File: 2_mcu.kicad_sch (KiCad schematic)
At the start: 33 parts, among them J201 Conn_01x05_Pin, J202 SWD TagConnect, SW201 PTS810 SJK, U201 STM32F446RETx, Y201 16MHz

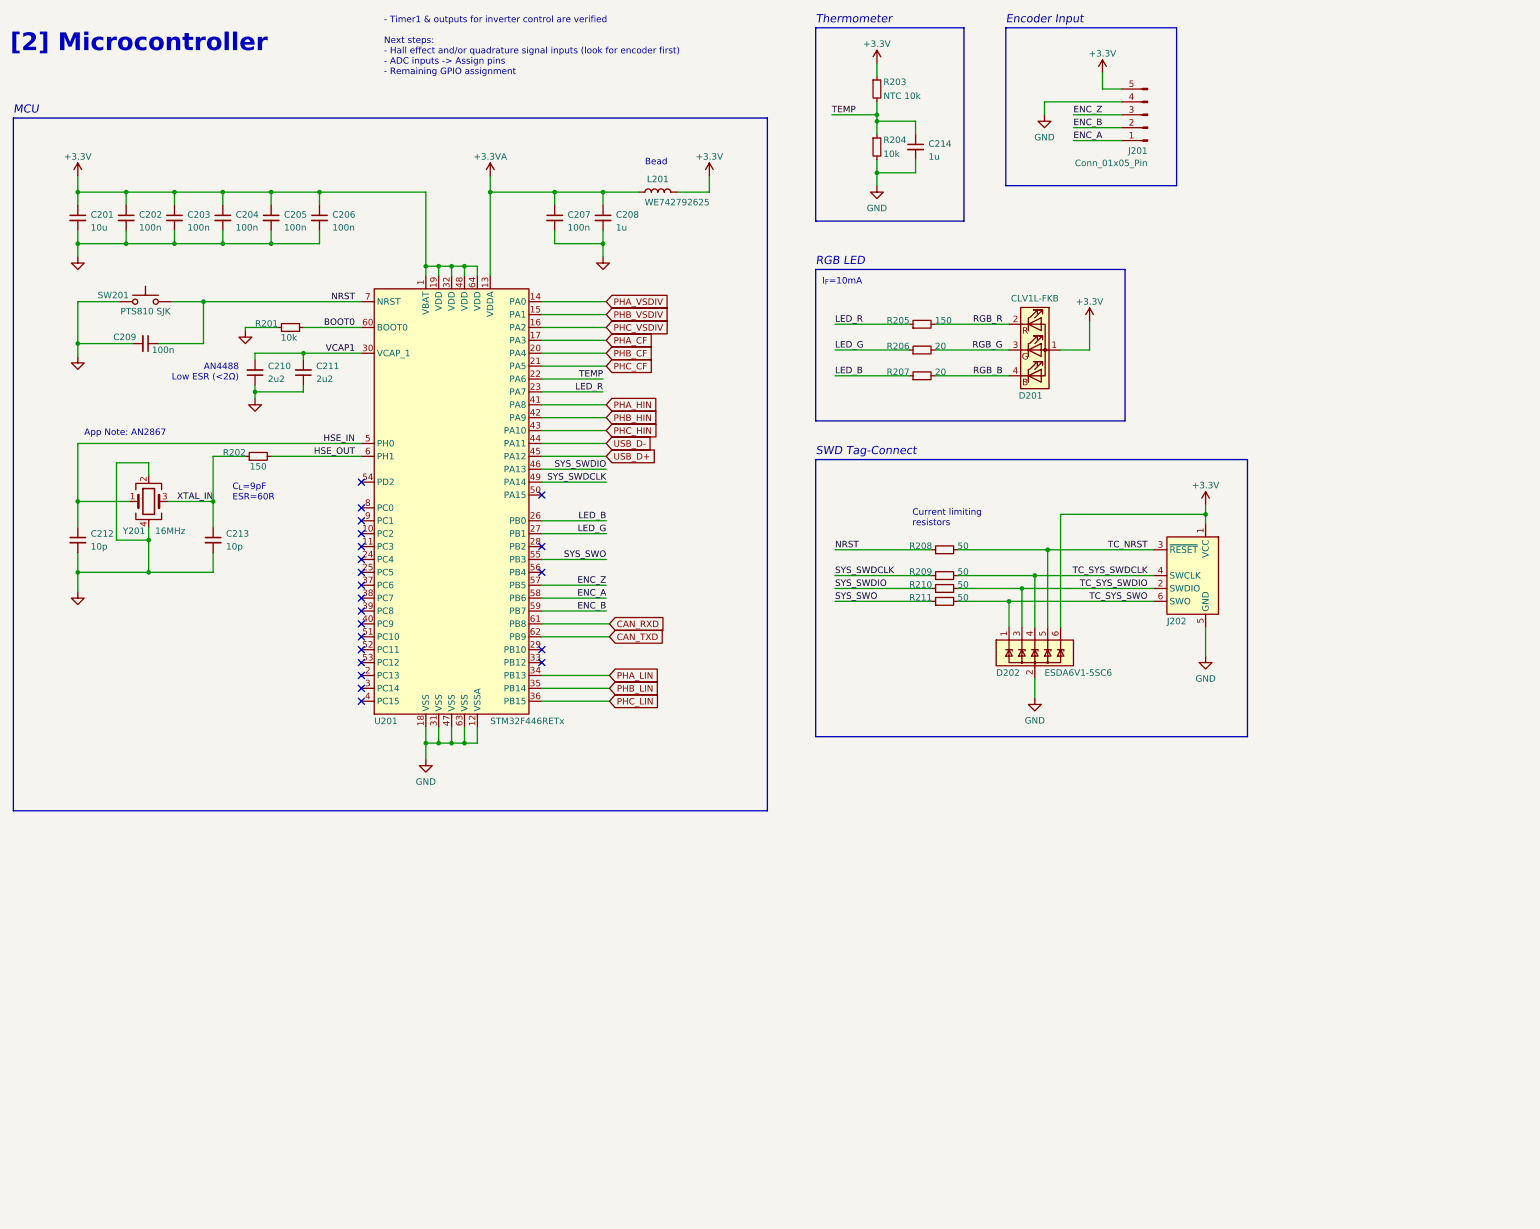
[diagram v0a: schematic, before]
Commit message: feat: major circuit rework, style update and addition of a few extra subcomponents
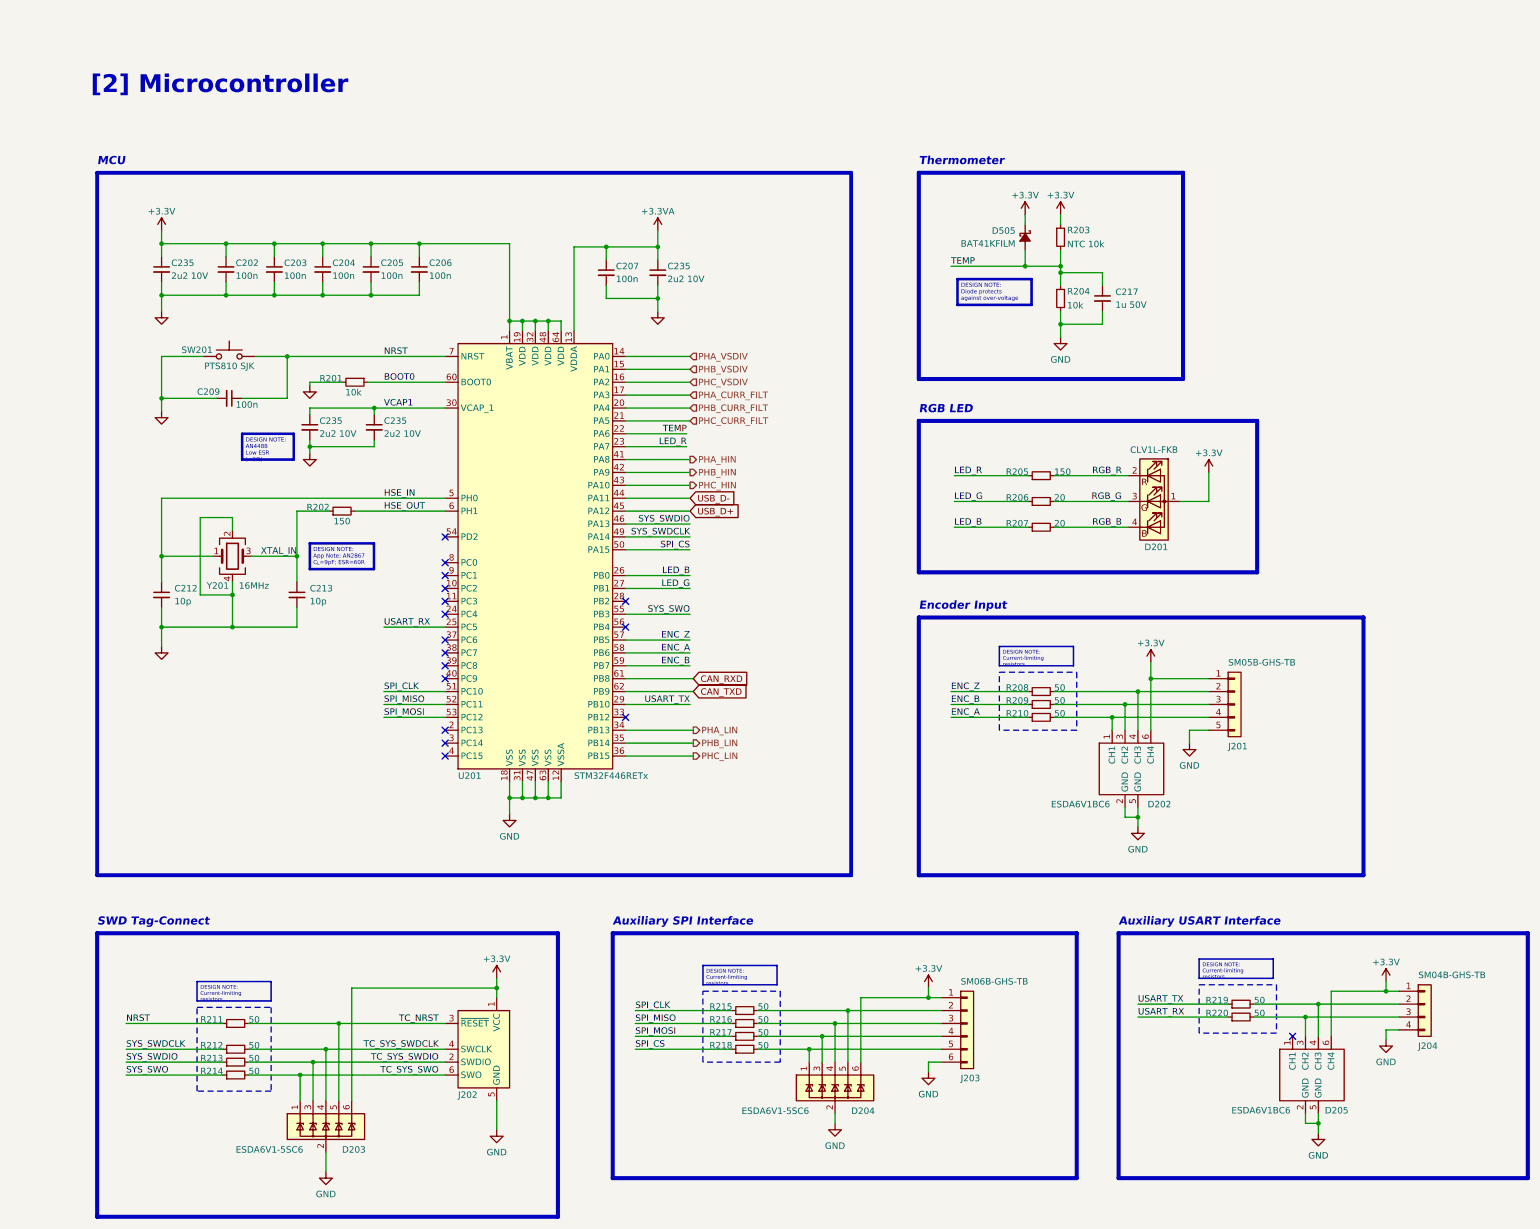
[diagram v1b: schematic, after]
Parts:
- removed C201: 10u, Capacitor_SMD:C_0603_1608Metric_Pad1.08x0.95mm_HandSolder, symbol Device:C_Small
- removed C208, C214: 1u, Capacitor_SMD:C_0603_1608Metric_Pad1.08x0.95mm_HandSolder, symbol Device:C_Small
- removed C210, C211: 2u2, Capacitor_SMD:C_0603_1608Metric_Pad1.08x0.95mm_HandSolder, symbol Device:C_Small
- removed J201: Conn_01x05_Pin, Connector_PinHeader_2.54mm:PinHeader_1x05_P2.54mm_Vertical, symbol Connector:Conn_01x05_Pin
- removed L201: WE742792625, Inductor_SMD:L_0603_1608Metric_Pad1.05x0.95mm_HandSolder, symbol Device:L
- added C217: 1u 50V, Capacitor_SMD:C_0603_1608Metric_Pad1.08x0.95mm_HandSolder, symbol Device:C_Small
- added C235 (x4): 2u2 10V, Capacitor_SMD:C_0603_1608Metric_Pad1.08x0.95mm_HandSolder, symbol Device:C_Small
- added D202, D205: ESDA6V1BC6, Package_TO_SOT_SMD:SOT-23-6, symbol Power_Protection:ESDA6V1BC6
- added D204: ESDA6V1-5SC6, Package_TO_SOT_SMD:SOT-23-6, symbol Power_Protection:ESDA6V1-5SC6
- added D505: BAT41KFILM, Diode_SMD:D_SOD-523, symbol Device:D_Schottky_Small_Filled
- added J201: SM05B-GHS-TB, Connector_JST:JST_GH_SM05B-GHS-TB_1x05-1MP_P1.25mm_Horizontal, symbol Connector_Generic:Conn_01x05
- added J203: SM06B-GHS-TB, Connector_JST:JST_GH_SM06B-GHS-TB_1x06-1MP_P1.25mm_Horizontal, symbol Connector_Generic:Conn_01x06
- added J204: SM04B-GHS-TB, Connector_JST:JST_GH_SM04B-GHS-TB_1x04-1MP_P1.25mm_Horizontal, symbol Connector_Generic:Conn_01x04
- added R208, R209, R210, R215, R216, R217, R218, R219, R220: 50, Resistor_SMD:R_0402_1005Metric_Pad0.72x0.64mm_HandSolder, symbol Device:R_Small
- D203: renamed from D202; Link https://www.mouser.de/ProductDetail/STMicroelectronics/ESDA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 -> https://www.digikey.de/en/products/detail/stmicroelectronic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
- renumbered R208 to R211, R209 to R212, R210 to R213, R211 to R214
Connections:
- net +3.3V: now also C235.1, D202.6 (CH4), D204.6 (IO5), D205.6 (CH4), D505.1 (K), J201.1 (Pin_1), J203.1 (Pin_1), J204.1 (Pin_1)
- net +3.3VA: now also C235.1
- net ENC_A: now also R210.1
- net ENC_B: now also R209.1
- net ENC_Z: now also R208.1
- net GND: now also C217.2, C235.2, C235.2, C235.2, C235.2, D202.2 (GND), D202.5 (GND), D204.2 (GND), D205.2 (GND), D205.5 (GND), J201.5 (Pin_5), J203.6 (Pin_6), J204.4 (Pin_4)
- net TEMP: now also C217.1, D505.2 (A)
- net VCAP1: now also C235.1, C235.1
- net USART_RX: now reaches U201.25 (PC5)
- net USART_RX: now also R220.1
- net USART_TX: now reaches U201.29 (PB10)
- net USART_TX: now also R219.1
- net SPI_CS: now reaches U201.50 (PA15)
- net SPI_CS: now also R218.1
- net SPI_CLK: now reaches U201.51 (PC10)
- net SPI_CLK: now also R215.1
- net SPI_MISO: now reaches U201.52 (PC11)
- net SPI_MISO: now also R216.1
- net SPI_MOSI: now reaches U201.53 (PC12)
- net SPI_MOSI: now also R217.1
- net PHA_CF renamed PHA_CURR_FILT
- net PHB_CF renamed PHB_CURR_FILT
- net PHC_CF renamed PHC_CURR_FILT
- new net: D204.1 (IO1), J203.5 (Pin_5), R218.2
- new net: D204.4 (IO3), J203.3 (Pin_3), R216.2
- new net: D205.4 (CH3), J204.2 (Pin_2), R219.2
- new net: D205.3 (CH2), J204.3 (Pin_3), R220.2
- new net: D202.4 (CH3), J201.2 (Pin_2), R208.2
- new net: D202.3 (CH2), J201.3 (Pin_3), R209.2
- new net: D202.1 (CH1), J201.4 (Pin_4), R210.2
- new net: D204.3 (IO2), J203.4 (Pin_4), R217.2
- new net: D204.5 (IO4), J203.2 (Pin_2), R215.2
- no-connect marks 22 -> 17
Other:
- note added: "Auxiliary SPI Interface"
- note added: "Auxiliary USART Interface"
- note removed: "- Timer1 & outputs for inverter control are verified Next steps: - Hall effect and/or quadrature signal inputs (look for encoder first) - ADC inputs -> Assign pins - Remaining GPIO assignment"
- note removed: "AN4488 Low ESR (<2Ω)"
- note removed: "App Note: AN2867"
- note removed: "Bead"
- note removed: "C_{L}=9pF ESR=60R"
- note removed: "Current limiting resistors"
- note removed: "I_{F}=10mA"
- moved on the sheet: C202, C203, C204, C205, C206, C207, C209, C212, C213, D201, D203, J202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

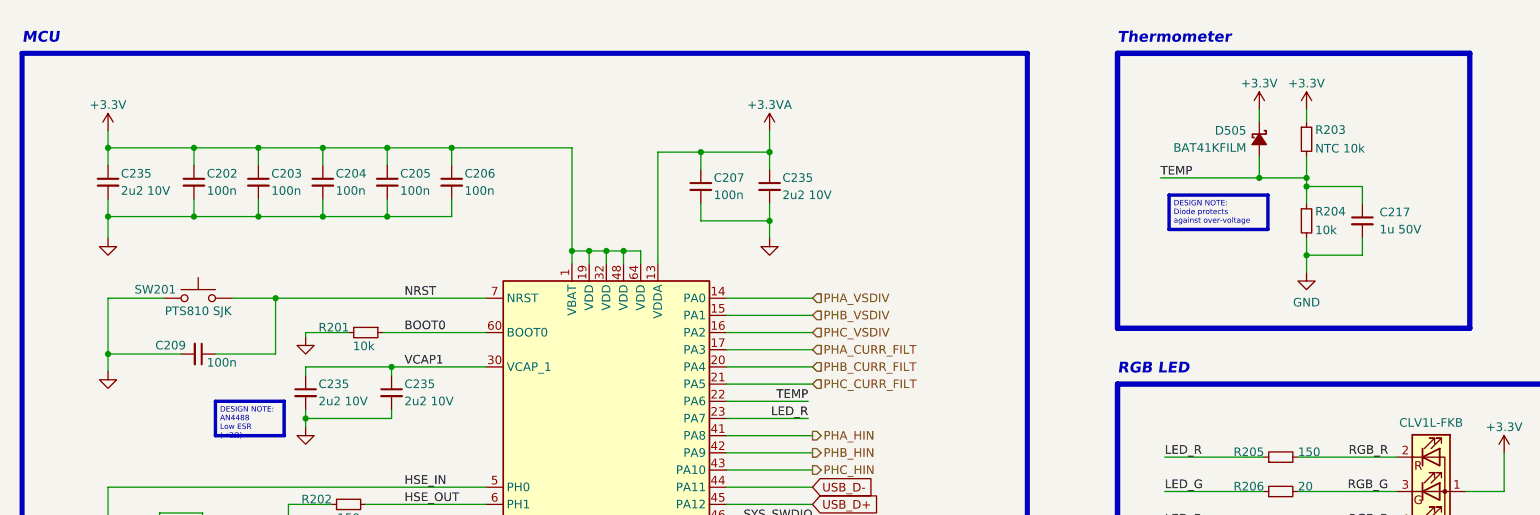
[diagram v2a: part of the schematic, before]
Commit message: feat: finished inverter placement and routing
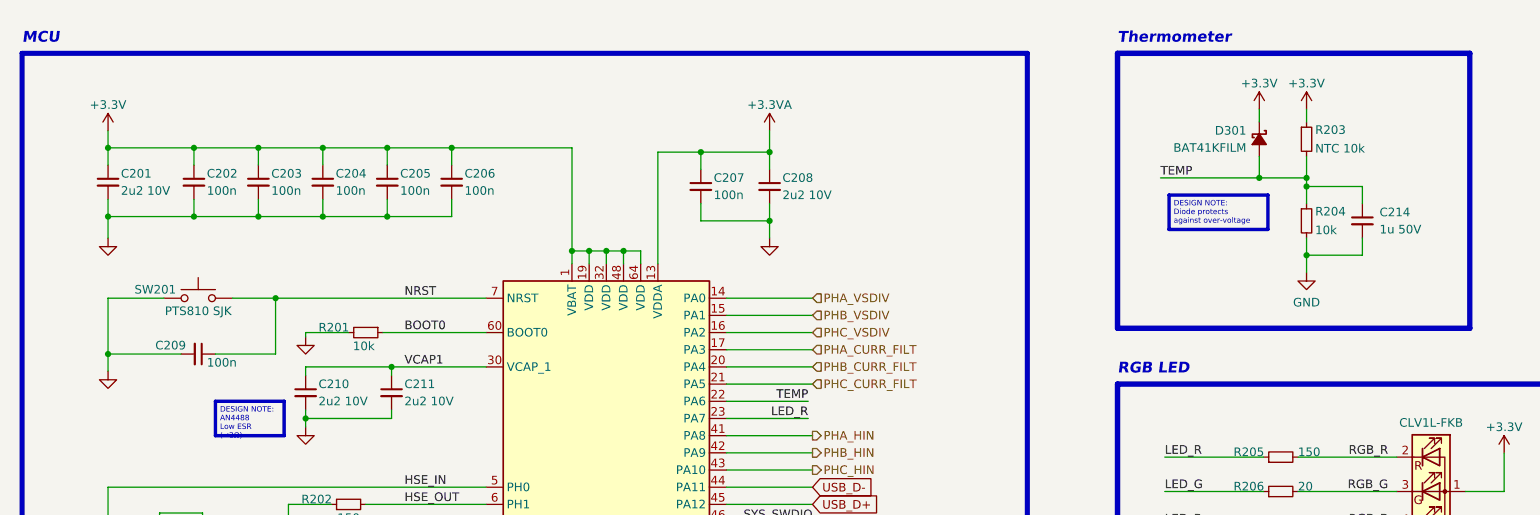
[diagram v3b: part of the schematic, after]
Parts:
- renumbered C235 to C201, C235 to C208, C235 to C210, C235 to C211, C217 to C214, D505 to D301
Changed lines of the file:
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@@
   (symbol (lib_id "Device:C_Small") (at 146.05 68.58 0) (unit 1)
     (in_bom yes) (on_board yes) (dnp no)
-    (property "Reference" "C235" (at 147.955 67.31 0)
+    (property "Reference" "C208" (at 147.955 67.31 0)
       (effects (font (size 1.27 1.27)) (justify left))
     )
@@
     (instances
       (project "ESC_R1"
-        (path "/9dea2e18-5867-4ed4-a12d-7ee109225de0/bab0431c-ca33-4c57-9dbe-00ccaf05ca0f"
-          (reference "C235") (unit 1)
-        )
         (path "/9dea2e18-5867-4ed4-a12d-7ee109225de0/52041989-aba3-4113-ba04-ece39669328f"
           (reference "C208") (unit 1)
@@
   (symbol (lib_id "Device:C_Small") (at 233.68 73.66 0) (unit 1)
     (in_bom yes) (on_board yes) (dnp no)
-    (property "Reference" "C217" (at 236.22 72.39 0)
+    (property "Reference" "C214" (at 236.22 72.39 0)
       (effects (font (size 1.27 1.27)) (justify left))
     )
@@
     (instances
       (project "ESC_R1"
-        (path "/9dea2e18-5867-4ed4-a12d-7ee109225de0/bab0431c-ca33-4c57-9dbe-00ccaf05ca0f"
-          (reference "C217") (unit 1)
-        )
         (path "/9dea2e18-5867-4ed4-a12d-7ee109225de0/52041989-aba3-4113-ba04-ece39669328f"
           (reference "C214") (unit 1)
@@
   (symbol (lib_id "power:+3.3V") (at 218.44 57.15 0) (unit 1)
     (in_bom yes) (on_board yes) (dnp no)
-    (property "Reference" "#PWR0146" (at 218.44 60.96 0)
+    (property "Reference" "#PWR0301" (at 218.44 60.96 0)
       (effects (font (size 1.27 1.27)) hide)
     )
@@
     (instances
       (project "ESC_R1"
-        (path "/9dea2e18-5867-4ed4-a12d-7ee109225de0/a82201a8-9dca-4a1d-828e-2de3fb3c1adb"
-          (reference "#PWR0146") (unit 1)
-        )
-        (path "/9dea2e18-5867-4ed4-a12d-7ee109225de0/fe2fcbfe-ce2b-4fee-9243-f26c3dcbcd78"
-          (reference "#PWR0707") (unit 1)
-        )
-        (path "/9dea2e18-5867-4ed4-a12d-7ee109225de0/4eb0e494-3187-44db-9d3d-24d2fbf5dea7"
-          (reference "#PWR0807") (unit 1)
-        )
         (path "/9dea2e18-5867-4ed4-a12d-7ee109225de0/52041989-aba3-4113-ba04-ece39669328f"
           (reference "#PWR0301") (unit 1)
@@
   (symbol (lib_id "Device:D_Schottky_Small_Filled") (at 218.44 61.595 270) (unit 1)
     (in_bom yes) (on_board yes) (dnp no)
-    (property "Reference" "D505" (at 216.535 60.325 90)
+    (property "Reference" "D301" (at 216.535 60.325 90)
       (effects (font (size 1.27 1.27)) (justify right))
     )
@@
     (instances
       (project "ESC_R1"
-        (path "/9dea2e18-5867-4ed4-a12d-7ee109225de0/a82201a8-9dca-4a1d-828e-2de3fb3c1adb"
-          (reference "D505") (unit 1)
-        )
-        (path "/9dea2e18-5867-4ed4-a12d-7ee109225de0/fe2fcbfe-ce2b-4fee-9243-f26c3dcbcd78"
-          (reference "D702") (unit 1)
-        )
-        (path "/9dea2e18-5867-4ed4-a12d-7ee109225de0/4eb0e494-3187-44db-9d3d-24d2fbf5dea7"
-          (reference "D?") (unit 1)
-        )
         (path "/9dea2e18-5867-4ed4-a12d-7ee109225de0/52041989-aba3-4113-ba04-ece39669328f"
           (reference "D301") (unit 1)
@@
   (symbol (lib_id "Device:C_Small") (at 48.26 67.945 0) (unit 1)
     (in_bom yes) (on_board yes) (dnp no)
-    (property "Reference" "C235" (at 50.165 66.675 0)
+    (property "Reference" "C201" (at 50.165 66.675 0)
       (effects (font (size 1.27 1.27)) (justify left))
     )
@@
     (instances
       (project "ESC_R1"
-        (path "/9dea2e18-5867-4ed4-a12d-7ee109225de0/bab0431c-ca33-4c57-9dbe-00ccaf05ca0f"
-          (reference "C235") (unit 1)
-        )
         (path "/9dea2e18-5867-4ed4-a12d-7ee109225de0/52041989-aba3-4113-ba04-ece39669328f"
           (reference "C201") (unit 1)
@@
   (symbol (lib_id "Device:C_Small") (at 90.17 99.06 0) (unit 1)
     (in_bom yes) (on_board yes) (dnp no)
-    (property "Reference" "C235" (at 92.075 97.79 0)
+    (property "Reference" "C211" (at 92.075 97.79 0)
       (effects (font (size 1.27 1.27)) (justify left))
     )
@@
     (instances
       (project "ESC_R1"
-        (path "/9dea2e18-5867-4ed4-a12d-7ee109225de0/bab0431c-ca33-4c57-9dbe-00ccaf05ca0f"
-          (reference "C235") (unit 1)
-        )
         (path "/9dea2e18-5867-4ed4-a12d-7ee109225de0/52041989-aba3-4113-ba04-ece39669328f"
           (reference "C211") (unit 1)
@@
   (symbol (lib_id "Device:C_Small") (at 77.47 99.06 0) (unit 1)
     (in_bom yes) (on_board yes) (dnp no)
-    (property "Reference" "C235" (at 79.375 97.79 0)
+    (property "Reference" "C210" (at 79.375 97.79 0)
       (effects (font (size 1.27 1.27)) (justify left))
     )
@@
     (instances
       (project "ESC_R1"
-        (path "/9dea2e18-5867-4ed4-a12d-7ee109225de0/bab0431c-ca33-4c57-9dbe-00ccaf05ca0f"
-          (reference "C235") (unit 1)
-        )
         (path "/9dea2e18-5867-4ed4-a12d-7ee109225de0/52041989-aba3-4113-ba04-ece39669328f"
           (reference "C210") (unit 1)
